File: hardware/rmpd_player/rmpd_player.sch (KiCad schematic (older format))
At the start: 112 parts, among them J1 POWER, J2 PROG, J3 LINE_OUT_INT_1, J4 LINE_OUT, J5 MICRO_SD, J6 POWER_INT, J7 LINE_OUT_INT_2, J8 RESERV, Q1 BC848, Q2 BC848, Q3 BC858, Q4 BC858, U1 DS3231M, U2 VS1011E, U3 LM1117-3.3, U4 ESP32-WROOM, U5 RC4558, U6 RC4558, U7 RC4558, Y1 12.288MHz

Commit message: wip: new tps54331 power
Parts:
- removed C17, C18: 10.0, Capacitors_THT:CP_Radial_D5.0mm_P2.50mm, symbol Device:CP
- removed D1: 5.1V, Diodes_THT:D_A-405_P7.62mm_Horizontal, symbol Device:D_Zener
- added C17, C18, C46, C47: 0.01, Capacitors_SMD:C_0805_HandSoldering, symbol Device:C
- added C40, C41: 1000pF, Capacitors_SMD:C_0805_HandSoldering, symbol Device:C
- added C42, C43: 10.0, Capacitors_THT:CP_Radial_D5.0mm_P2.50mm, symbol Device:CP
- added C44, C45: 47pF, Capacitors_SMD:C_0805_HandSoldering, symbol Device:C
- added C48, C49: 100n, Capacitors_SMD:C_0805_HandSoldering, symbol Device:C
- added C50, C51, C52, C53: 47uF, Capacitors_SMD:C_1206_HandSoldering, symbol Device:C
- added D1, D3: B340, Opto-Devices:PhotoDiode_SMD-DIL2_4.5x4, symbol Diode:B340
- added L1, L2: 6.8uH, Inductors_SMD:L_6.3x6.3_H3, symbol Device:L_Core_Ferrite
- added R50, R51: 30k, Resistors_SMD:R_0805_HandSoldering, symbol Device:R
- added R52: 15k, Resistors_SMD:R_0805_HandSoldering, symbol Device:R
- added R53: 4k7, Resistors_SMD:R_0805_HandSoldering, symbol Device:R
- added R54: 10k, Resistors_SMD:R_0805_HandSoldering, symbol Device:R
- added R55: 1k6, Resistors_SMD:R_0805_HandSoldering, symbol Device:R
- added U8, U9: TPS54331D, Housings_SOIC:SOIC-8_3.9x4.9mm_Pitch1.27mm, symbol Regulator_Switching:TPS54233
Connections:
- net labels added: VDDA_OP, VDDA_VS, VDD_ESP, VDD_VS, VIN, VIN_UNFUSED
- net labels removed: 5V, VDD, VDDA
- wire segments 475 -> 575
- no-connect marks 10 -> 12
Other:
- moved on the sheet: BT1, C1, C10, C11, C12, C13, C14, C15, C16, C19, C2, C20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

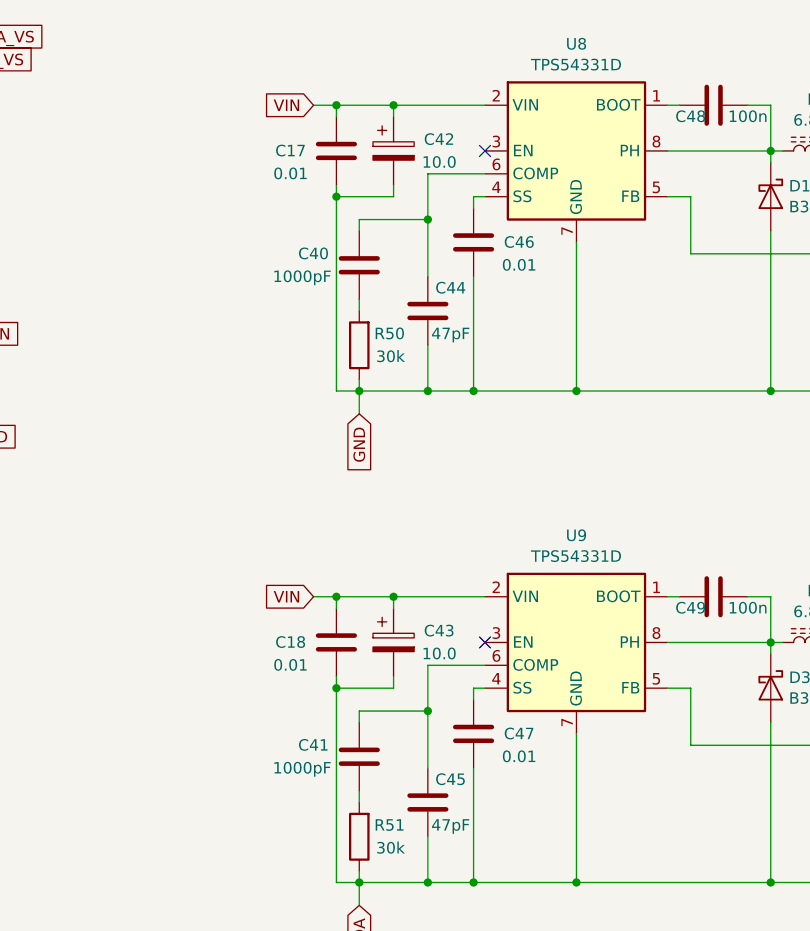
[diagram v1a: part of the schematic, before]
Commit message: equlize some capacitors values
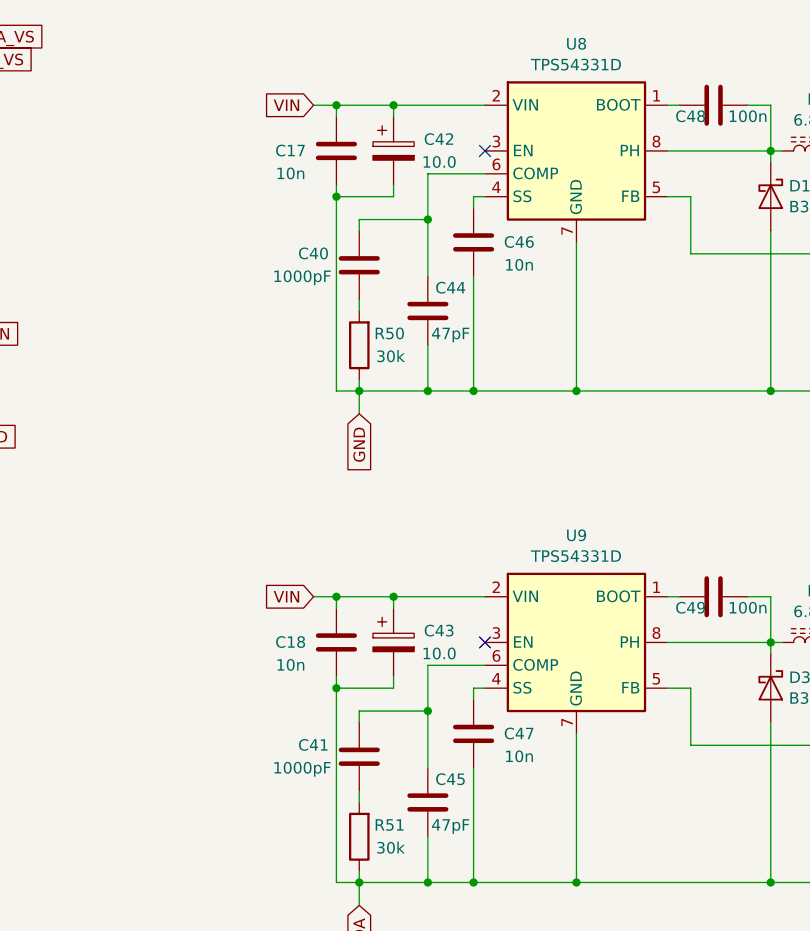
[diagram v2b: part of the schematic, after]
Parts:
- C17, C18, C46, C47: value 0.01 -> 10n
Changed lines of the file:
@@
 P 4300 7400
 F 0 "C17" H 4100 7400 50  0000 C CNN
-F 1 "0.01" H 4100 7300 50  0000 C CNN
+F 1 "10n" H 4100 7300 50  0000 C CNN
 F 2 "Capacitors_SMD:C_0805_HandSoldering" H 4338 7250 50  0001 C CNN
 F 3 "~" H 4300 7400 50  0001 C CNN
@@
 P 4900 7800
 F 0 "C46" H 5100 7800 50  0000 C CNN
-F 1 "0.01" H 5100 7700 50  0000 C CNN
+F 1 "10n" H 5100 7700 50  0000 C CNN
 F 2 "Capacitors_SMD:C_0805_HandSoldering" H 4938 7650 50  0001 C CNN
 F 3 "~" H 4900 7800 50  0001 C CNN
@@
 P 4300 9550
 F 0 "C18" H 4100 9550 50  0000 C CNN
-F 1 "0.01" H 4100 9450 50  0000 C CNN
+F 1 "10n" H 4100 9450 50  0000 C CNN
 F 2 "Capacitors_SMD:C_0805_HandSoldering" H 4338 9400 50  0001 C CNN
 F 3 "~" H 4300 9550 50  0001 C CNN
@@
 P 4900 9950
 F 0 "C47" H 5100 9950 50  0000 C CNN
-F 1 "0.01" H 5100 9850 50  0000 C CNN
+F 1 "10n" H 5100 9850 50  0000 C CNN
 F 2 "Capacitors_SMD:C_0805_HandSoldering" H 4938 9800 50  0001 C CNN
 F 3 "~" H 4900 9950 50  0001 C CNN

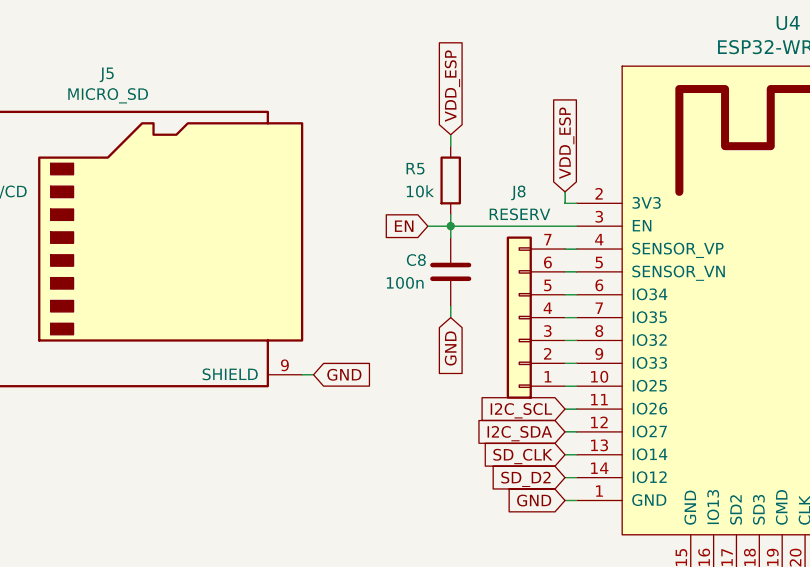
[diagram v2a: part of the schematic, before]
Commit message: change reset capacitor to 1uF
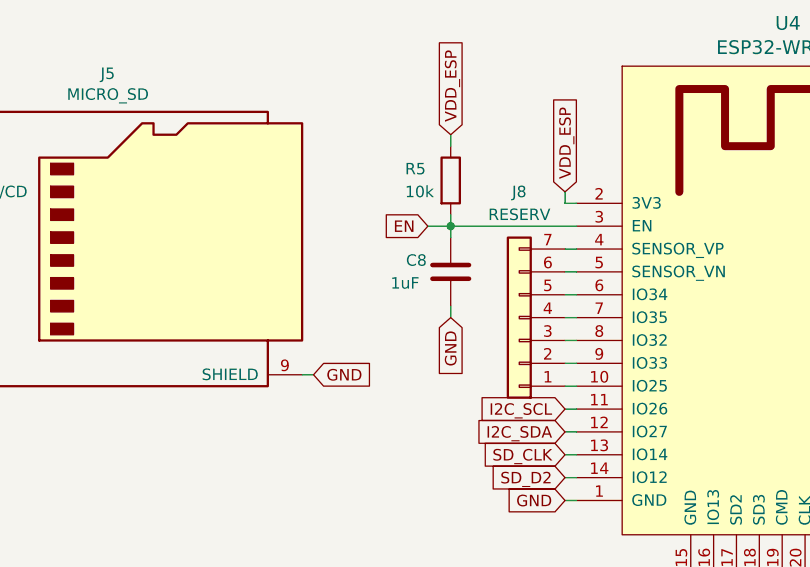
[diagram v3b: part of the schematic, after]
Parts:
- C8: value 100n -> 1uF
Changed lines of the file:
@@
 P 4000 1900
 F 0 "C8" H 4150 1850 50  0000 C CNN
-F 1 "100n" H 4200 1950 50  0000 C CNN
+F 1 "1uF" H 4200 1950 50  0000 C CNN
 F 2 "Capacitors_SMD:C_0805_HandSoldering" H 4038 1750 50  0001 C CNN
 F 3 "~" H 4000 1900 50  0001 C CNN

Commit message: kicad update
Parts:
- J5: symbol Connector:Micro_SD_Card -> rmpd_player-rescue:Micro_SD_Card-Connector
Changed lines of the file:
@@
 EESchema Schematic File Version 4
 LIBS:rmpd_player-cache
-EELAYER 26 0
+EELAYER 29 0
 EELAYER END
 $Descr A3 16535 11693
@@
 	15150 3850 15200 3850
 $Comp
-L Connector:Micro_SD_Card J5
+L rmpd_player-rescue:Micro_SD_Card-Connector J5
 U 1 1 5C2C64F7
 P 2550 1750

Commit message: update footprints to reflow
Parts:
- C1, C10, C11, C13, C14, C16, C17, C18, C2, C3, C37, C38, C39, C4, C40, C41, C44, C45, C46, C47, C48, C49, C5, C6, C7, C8, C9: footprint Capacitors_SMD:C_0805_HandSoldering -> Capacitors_SMD:C_0805
- C50, C51, C52, C53: footprint Capacitors_SMD:C_1206_HandSoldering -> Capacitors_SMD:C_1206
- F1: footprint Fuse_Holders_and_Fuses:Fuse_SMD1206_HandSoldering -> Fuse_Holders_and_Fuses:Fuse_SMD1206_Reflow
- R1, R10, R11, R12, R13, R14, R15, R16, R17, R18, R19, R2, R20, R21, R22, R23, R24, R25, R26, R27, R28, R29, R3, R30, R31, R32, R33, R34, R35, R36, R37, R38, R39, R4, R40, R41, R42, R43, R44, R45, R46, R47, R48, R49, R5, R50, R51, R52, R53, R54, R55, R6, R7, R8, R9: footprint Resistors_SMD:R_0805_HandSoldering -> Resistors_SMD:R_0805
